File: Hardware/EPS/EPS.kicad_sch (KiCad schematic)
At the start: 1 part

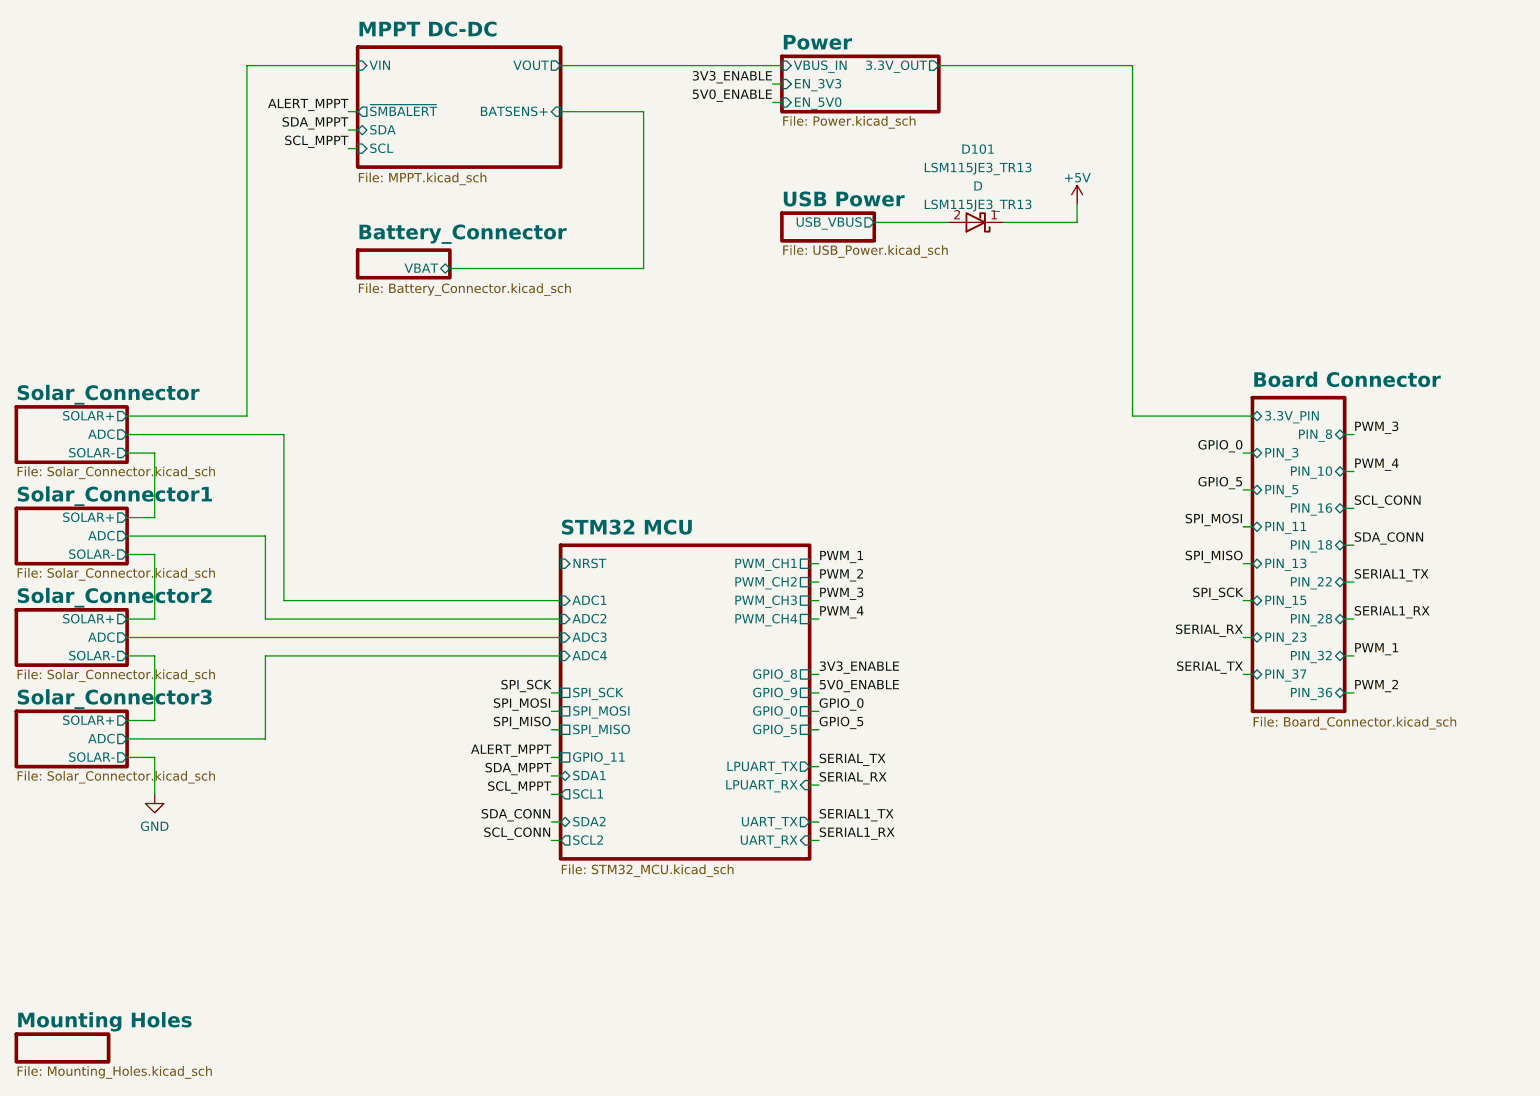
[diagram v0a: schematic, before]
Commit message: Changed uC pinout and finished uC routing
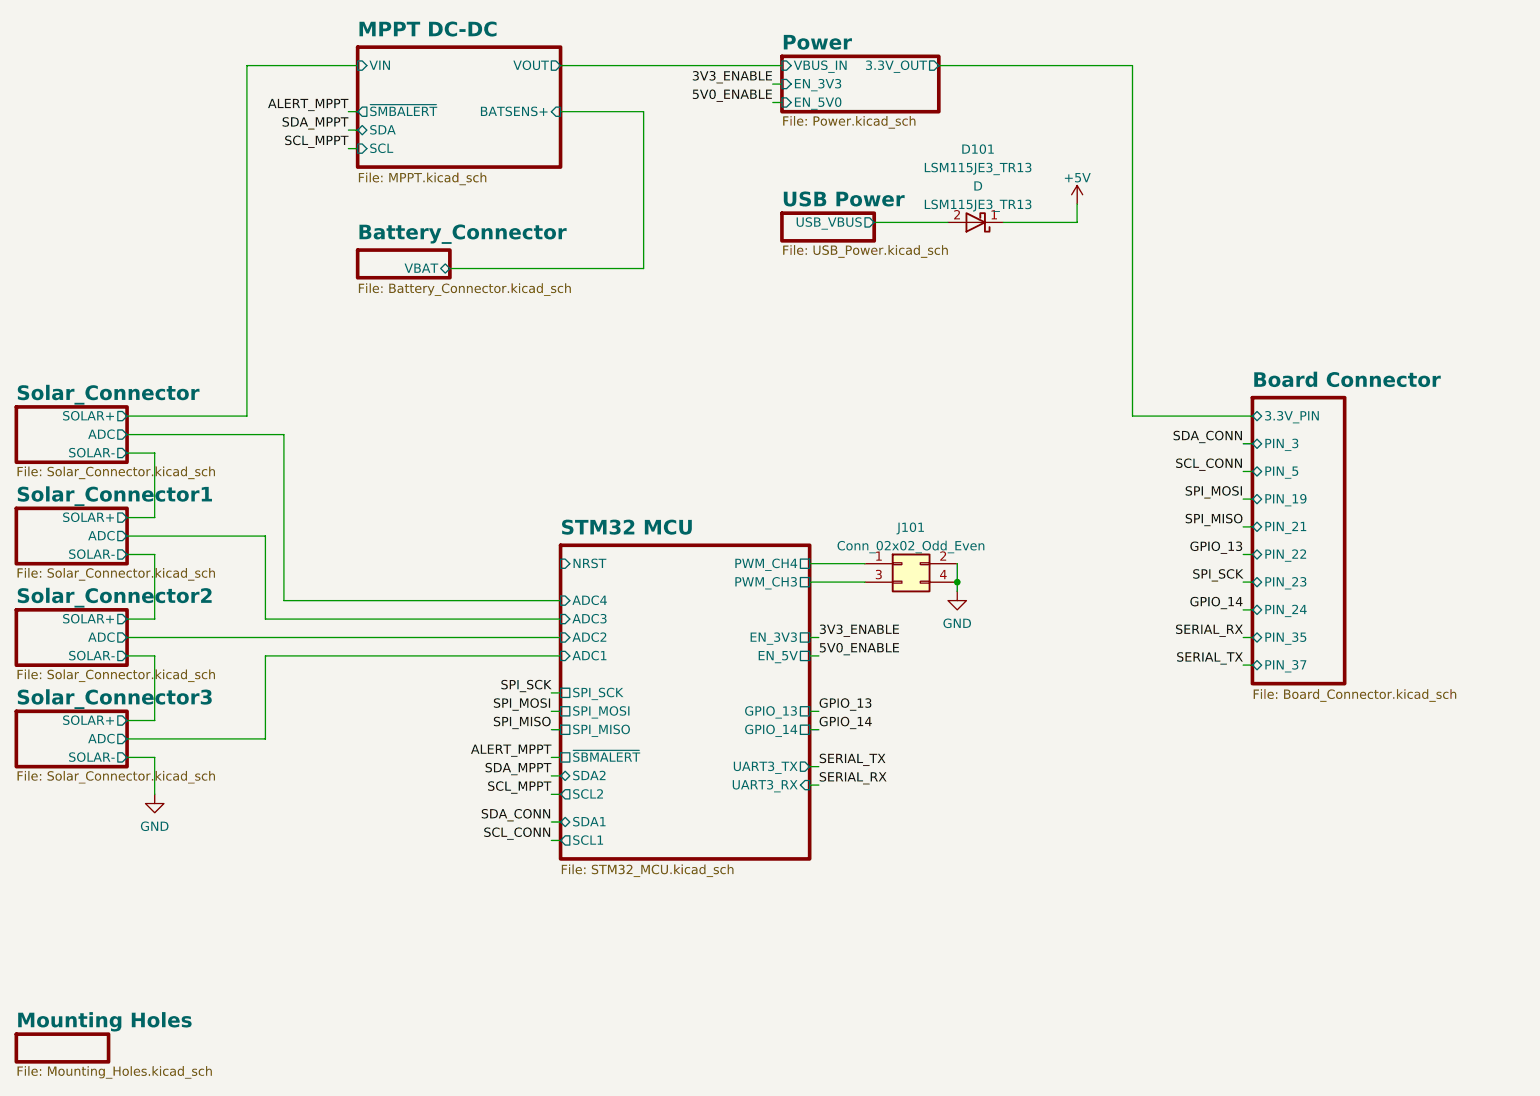
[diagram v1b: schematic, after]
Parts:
- added J101: Conn_02x02_Odd_Even, Connector_PinHeader_2.54mm:PinHeader_2x02_P2.54mm_Vertical, symbol Connector_Generic:Conn_02x02_Odd_Even
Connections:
- net GND: now also J101.2 (Pin_2), J101.4 (Pin_4)
- new net STM32 MCU/PWM_CH3: J101.3 (Pin_3)
- new net STM32 MCU/PWM_CH4: J101.1 (Pin_1)
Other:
- sheet Board Connector ports: added PIN_19, PIN_21, PIN_24, PIN_35; removed PIN_10, PIN_11, PIN_13, PIN_15, PIN_16, PIN_18, PIN_28, PIN_32, PIN_36, PIN_8
- sheet STM32 MCU ports: added EN_3V3, EN_5V, GPIO_13, GPIO_14, UART3_RX, UART3_TX, ~{SBMALERT}; removed GPIO_0, GPIO_11, GPIO_5, GPIO_8, GPIO_9, LPUART_RX, LPUART_TX, PWM_CH1, PWM_CH2, UART_RX, UART_TX

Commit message: Finished EPS - v0.1.0
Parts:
- added D102: BZT585B24T-7, Diode_SMD:D_SOD-523, symbol Device:D_Zener
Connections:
- net GND: now also D102.2 (A)
- net MPPT DC-DC/VIN: now also D102.1 (K)
